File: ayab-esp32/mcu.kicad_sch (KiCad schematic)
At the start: 34 parts, among them J201 SPARE1, J202 SPARE0, Q201 AO3400A, SW201 USER, SW202 RESET, SW203 BOOTSEL, U201 ESP32-S3-MINI-1

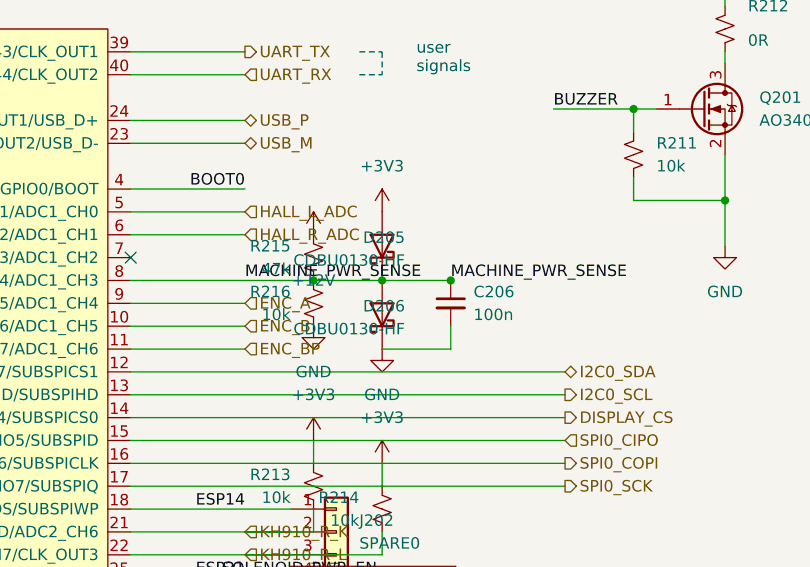
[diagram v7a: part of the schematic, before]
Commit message: Align clamp polarity and post-integration checks
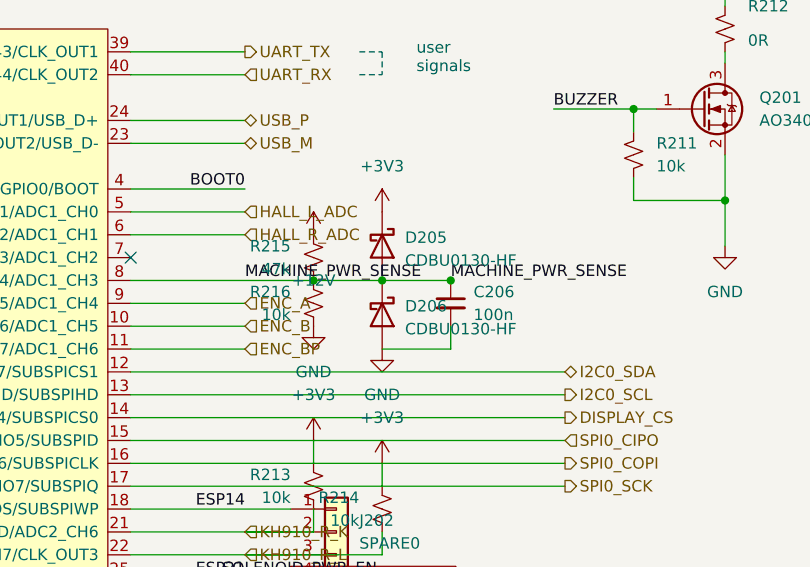
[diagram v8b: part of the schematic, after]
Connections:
- net +3V3: now also D205.1 (K); no longer D205.2 (A)
- net GND: now also D206.2 (A); no longer D206.1 (K)
- net MACHINE_PWR_SENSE: now also D205.2 (A), D206.1 (K); no longer D205.1 (K), D206.2 (A)
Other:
- moved on the sheet: D205, D206
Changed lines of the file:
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@@
     )
   )
-(symbol (lib_id "ayab-lib:D_Schottky") (at 213.36 78.74 90) (unit 1)
+(symbol (lib_id "ayab-lib:D_Schottky") (at 213.36 78.74 270) (unit 1)
     (in_bom yes) (on_board yes) (dnp no) (fields_autoplaced)
     (property "Reference" "D205" (at 215.9 77.7875 90)
@@
     )
   )
-(symbol (lib_id "ayab-lib:D_Schottky") (at 213.36 86.36 90) (unit 1)
+(symbol (lib_id "ayab-lib:D_Schottky") (at 213.36 86.36 270) (unit 1)
     (in_bom yes) (on_board yes) (dnp no) (fields_autoplaced)
     (property "Reference" "D206" (at 215.9 85.4075 90)
